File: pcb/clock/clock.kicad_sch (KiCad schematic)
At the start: 28 parts, among them J1 Conn_02x05_Odd_Even, Q1 Q_PMOS_GSD, Q2 Q_PMOS_GSD, Q3 Q_PMOS_GSD, Q4 HX2301A, SW1 SW_DIP_x01, SW2 SW_DIP_x01, U1 LSD080BAG-103A-01, U2 LSD080BAG-103A-01, U3 74HC595, U4 LSD080BAG-103A-01, U5 LSD080BAG-103A-01, U6 74HC595

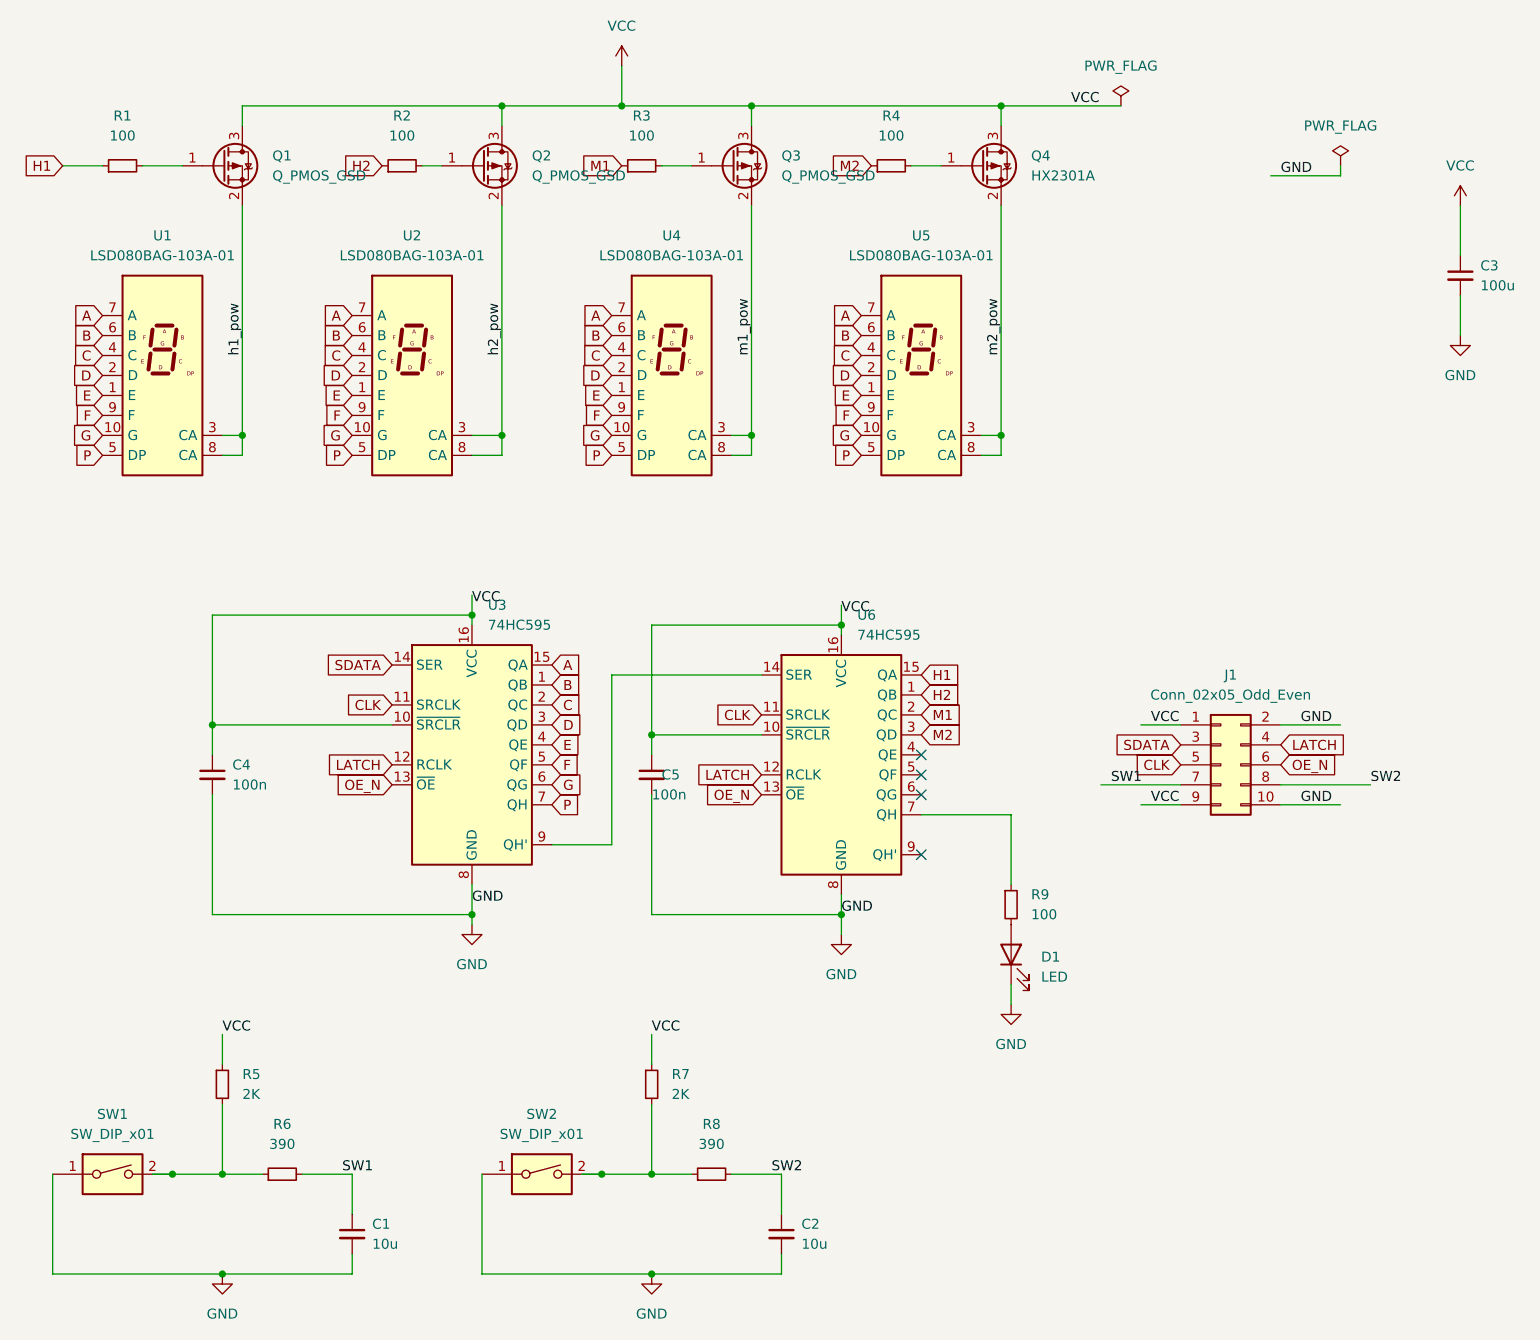
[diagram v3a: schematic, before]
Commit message: new version. tried to fix the busg in v1
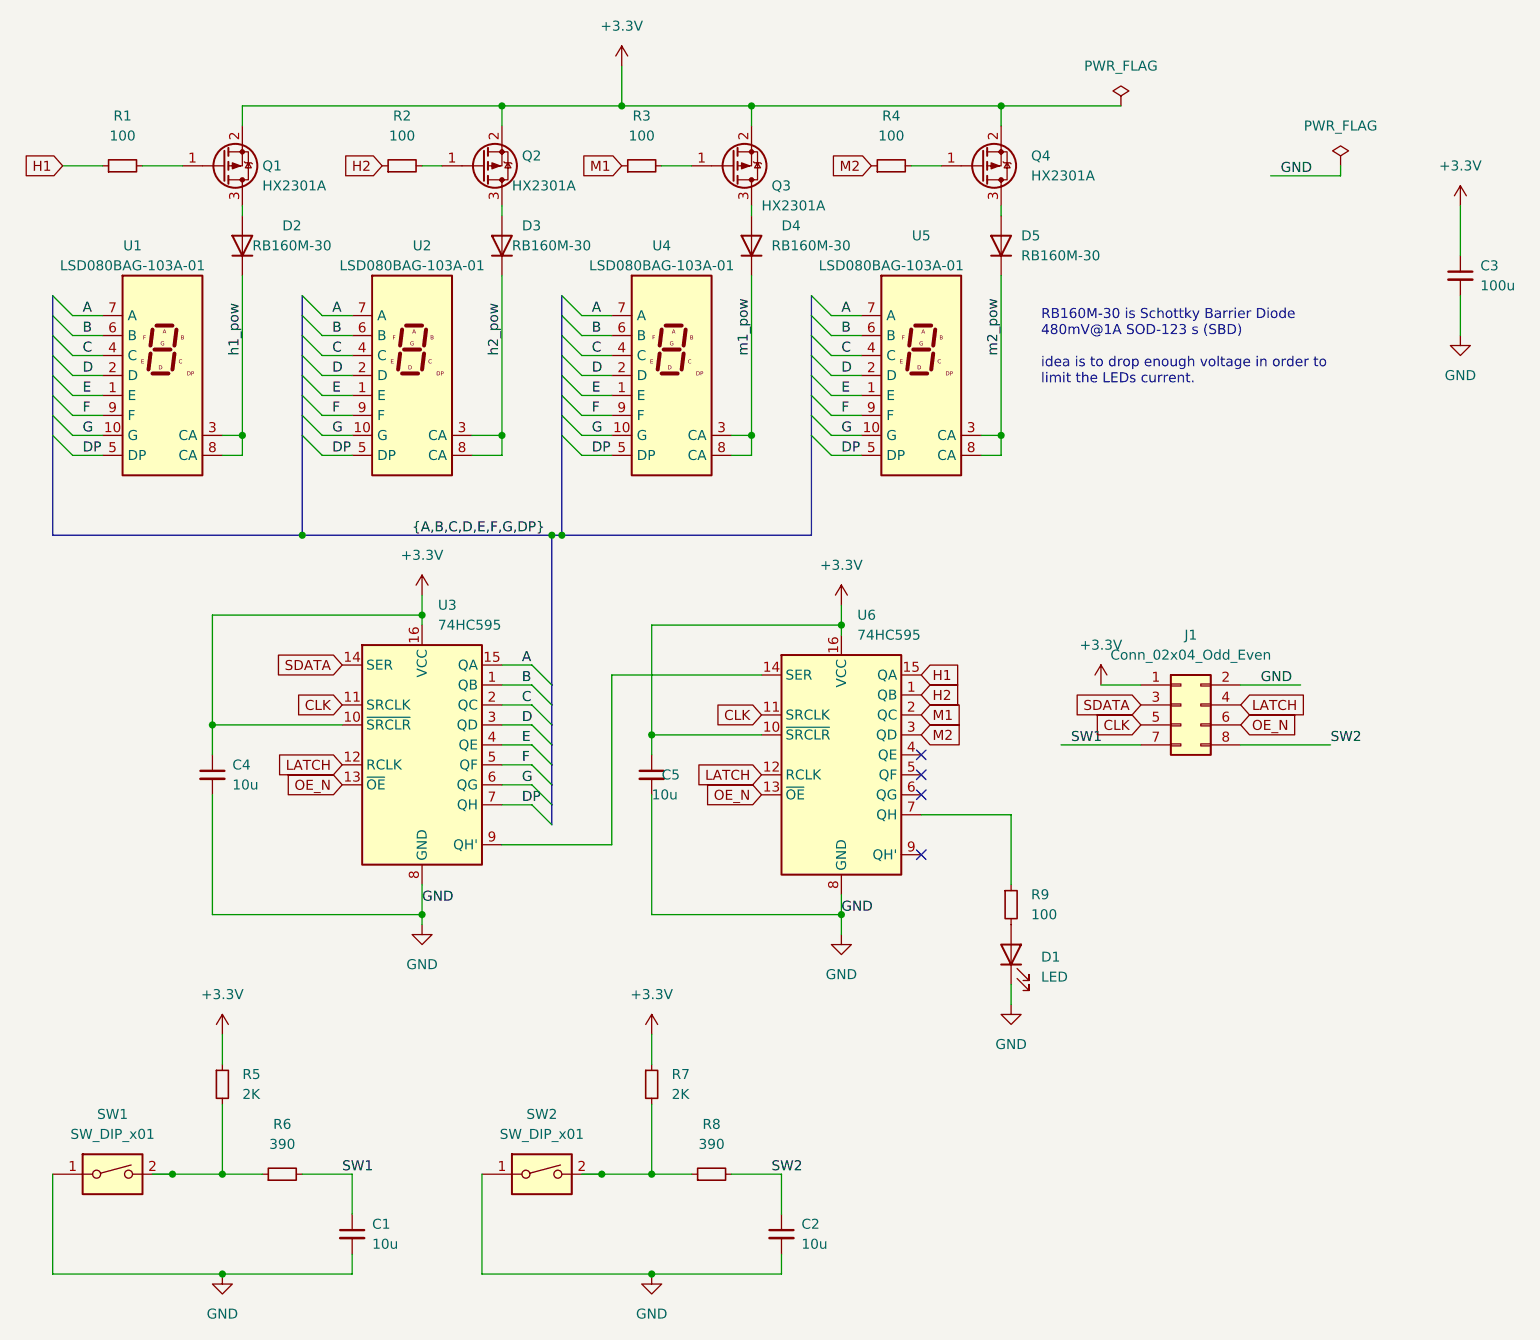
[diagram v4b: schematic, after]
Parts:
- removed J1: Conn_02x05_Odd_Even, Connector_PinHeader_2.54mm:PinHeader_2x05_P2.54mm_Vertical_SMD, symbol Connector_Generic:Conn_02x05_Odd_Even
- added D2, D3, D4, D5: RB160M-30, Diode_SMD:D_SOD-123, symbol Device:D
- added J1: Conn_02x04_Odd_Even, Connector_PinHeader_2.54mm:PinHeader_2x04_P2.54mm_Vertical_SMD, symbol Connector_Generic:Conn_02x04_Odd_Even
- C4, C5: value 100n -> 10u
- Q1, Q2, Q3: value Q_PMOS_GSD -> HX2301A
- U3: footprint Package_SO:SOIC-16_3.9x9.9mm_P1.27mm -> components:SOIC-16_3.9x9.9mm_P1.27mm_handsolder
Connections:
- net CLK: now also J1.5 (Pin_5)
- net GND: now also J1.2 (Pin_2)
- net LATCH: now also J1.4 (Pin_4)
- net OE_N: now also J1.6 (Pin_6)
- net SDATA: now also J1.3 (Pin_3)
- net SW1: now also J1.7 (Pin_7)
- net SW2: now also J1.8 (Pin_8)
- net h1_pow: now also D2.1 (K); no longer Q1.2 (S)
- net h2_pow: now also D3.1 (K); no longer Q2.2 (S)
- net m1_pow: now also D4.1 (K); no longer Q3.2 (S)
- net m2_pow: now also D5.1 (K); no longer Q4.2 (S)
- net P renamed DP
- net VCC renamed +3V3
- net +3V3: now also Q1.2 (S), Q2.2 (S), Q3.2 (S), Q4.2 (S), J1.1 (Pin_1); no longer Q1.3 (D), Q2.3 (D), Q3.3 (D), Q4.3 (D)
- new net: D4.2 (A), Q3.3 (D)
- new net: D3.2 (A), Q2.3 (D)
- new net: D5.2 (A), Q4.3 (D)
- new net: D2.2 (A), Q1.3 (D)
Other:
- note added: "RB160M-30 is Schottky Barrier Diode 480mV@1A SOD-123 s (SBD) idea is to drop enough voltage in order to limit the LEDs current."
- moved on the sheet: U3
